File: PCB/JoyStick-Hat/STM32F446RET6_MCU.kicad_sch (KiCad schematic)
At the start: 51 parts, among them J1 20021121-00010C4LF, J16 Conn_01x06, J2 BU2032SM-JJ-GTR, J3 0675031020, SW1 TL3301NF260QG, U1 STM32F446VETx, X1 ABM3B-8.000MHZ-B2-T, X2 ABS07-32.768KHZ-9-T

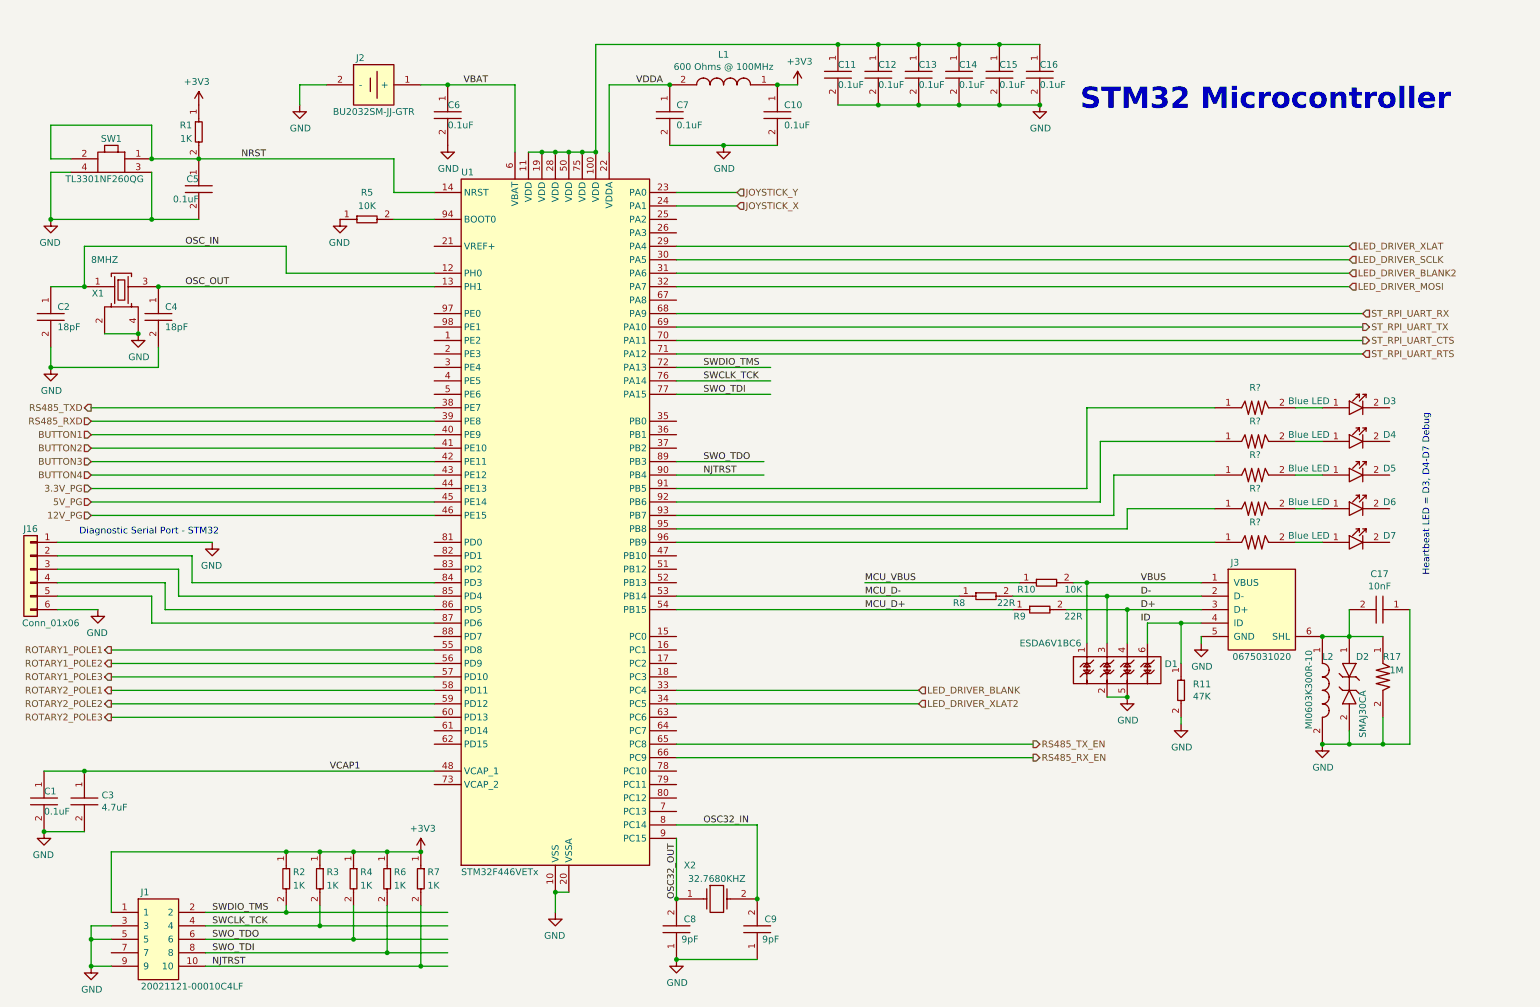
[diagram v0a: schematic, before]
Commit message: Design Rules, Component Placement. Features Dropped
Added design rules for OSHPark.com to PCB, Most components placed roughly for whole board more to follow and more tweaks,. Features were dropped/rearanged. USB for STM32 dropped as its not necessary. LED driver and LEDs will be on separate board and SPI will run through cabling via differential transceiver that has yet to be added to schematic.
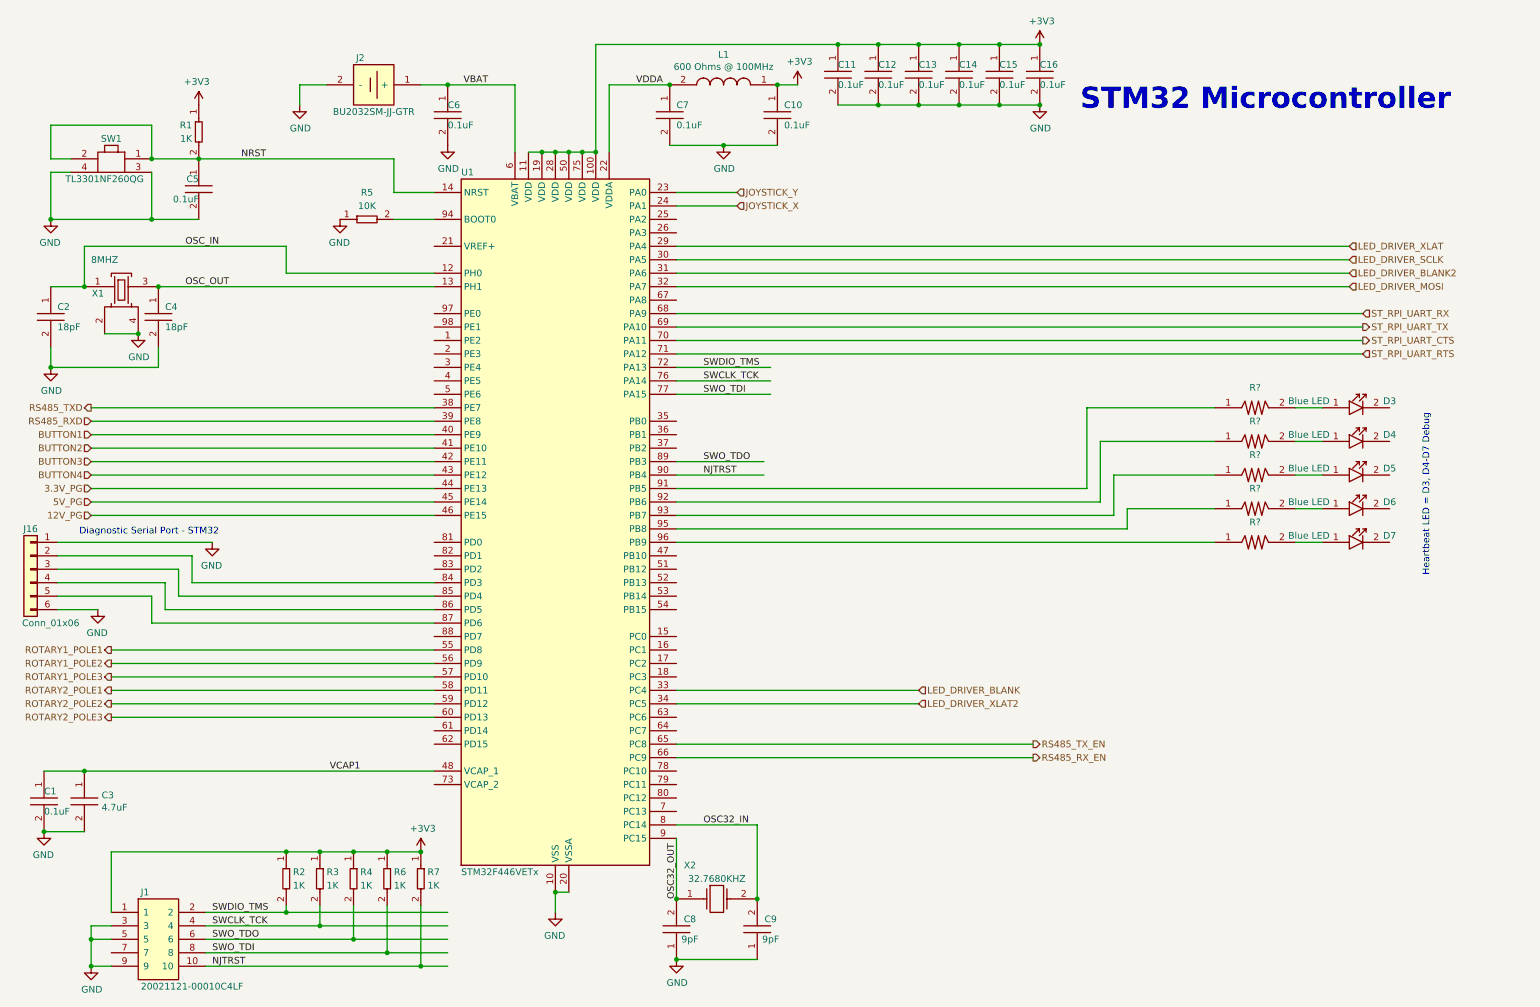
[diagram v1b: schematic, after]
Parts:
- removed C17: C0603X103K1RAC3316, AVR-KiCAD-Lib-Capacitors:C0603, symbol AVR-KiCAD-Lib-Capacitors:C0603X103K1RAC3316
- removed D1: ESDA6V1BC6, AVR-KiCAD-Lib-ICs:SOT-23-6_Handsoldering, symbol AVR-KiCAD-Lib-Diodes:ESDA6V1BC6
- removed D2: SMAJ30CA, AVR-KiCAD-Lib-Diodes:SMAJ30CA, symbol AVR-KiCAD-Lib-Diodes:SMAJ30CA
- removed J3: 0675031020, AVR-KiCAD-Lib-Connectors:USB_Mini-B, symbol AVR-KiCAD-Lib-Connectors:0675031020
- removed L2: MI0603K300R-10, AVR-KiCAD-Lib-Inductors:MI0603K300R-10, symbol AVR-KiCAD-Lib-Inductors:MI0603K300R-10
- removed R10: RC0402FR-0710KL, AVR-KiCAD-Lib-Resistors:R0402, symbol AVR-KiCAD-Lib-Resistors:RC0402FR-0710KL
- removed R11: RC0603FR-0747KL, AVR-KiCAD-Lib-Resistors:R0603, symbol AVR-KiCAD-Lib-Resistors:RC0603FR-0747KL
- removed R17: RC1206FR-071ML, AVR-KiCAD-Lib-Resistors:R1206, symbol AVR-KiCAD-Lib-Resistors:RC1206FR-071ML
- removed R8, R9: RC0402FR-0722RL, AVR-KiCAD-Lib-Resistors:R0402, symbol AVR-KiCAD-Lib-Resistors:RC0402FR-0722RL
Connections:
- net +3V3: now also C11.1, C12.1, C13.1, C14.1, C15.1, C16.1, U1.100 (VDD), U1.11 (VDD), U1.19 (VDD), U1.28 (VDD), U1.50 (VDD), U1.75 (VDD)
- net MCU_D+: no longer names the net of U1.54 (PB15)
- net MCU_D-: no longer names the net of U1.53 (PB14)

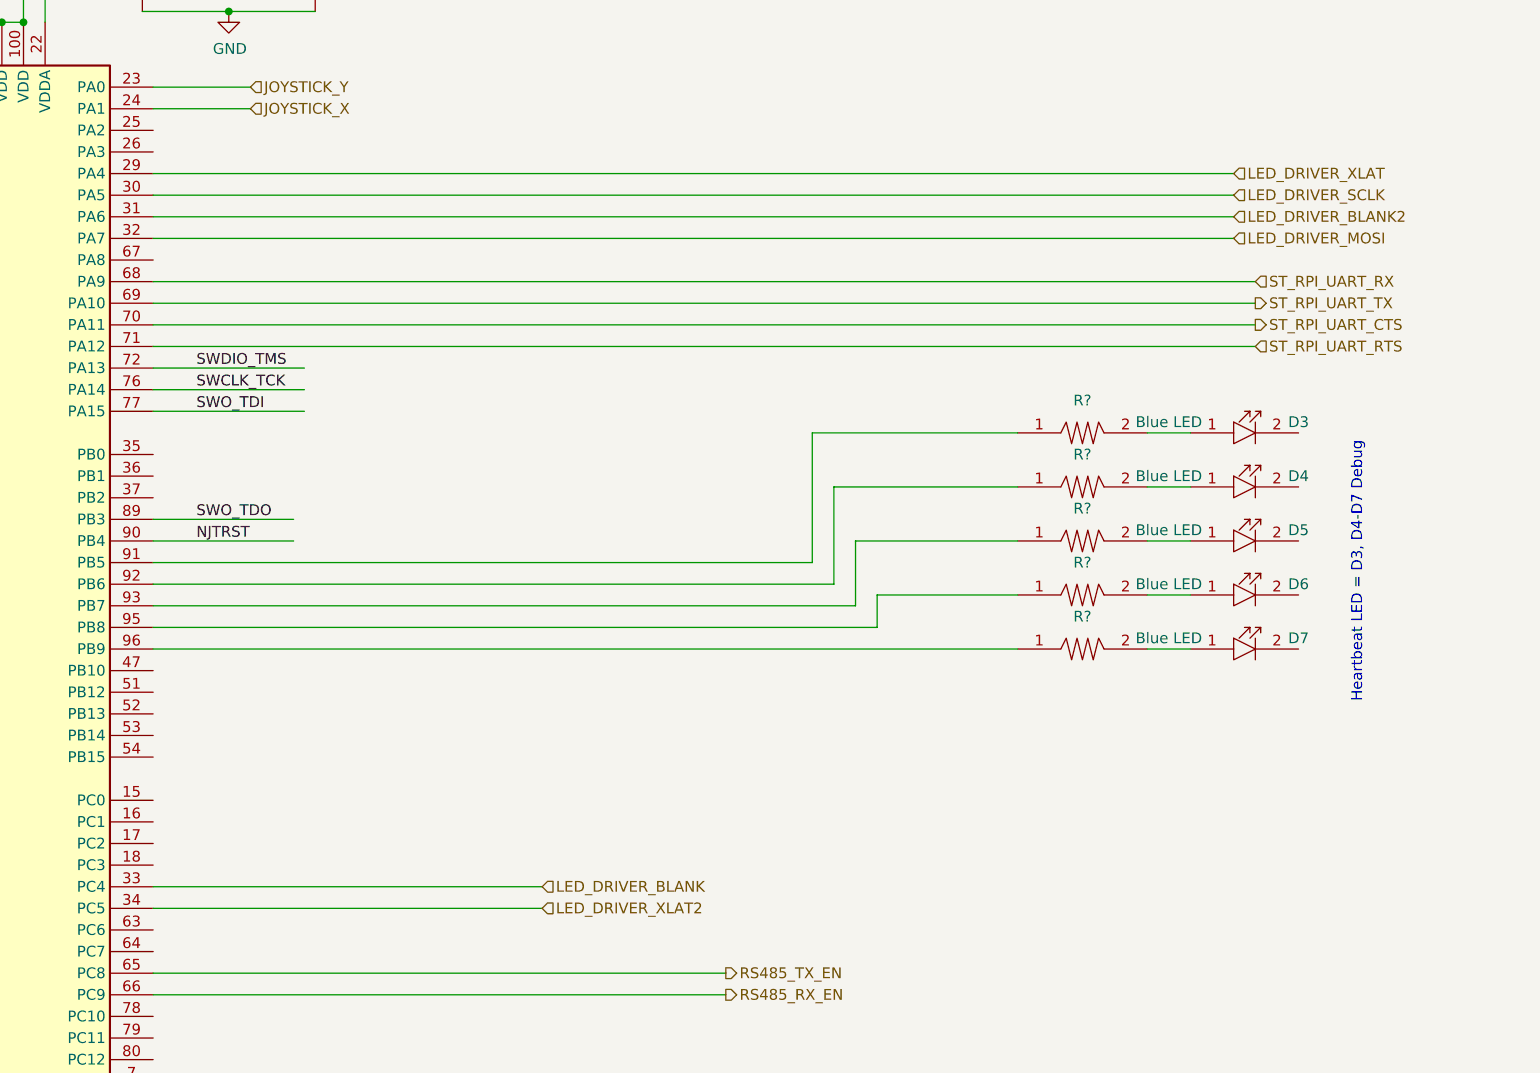
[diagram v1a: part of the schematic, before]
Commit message: Board Tweaks and progress
Made progress with baord. Adjusted the position of RPi header to be correct and absolute. Changed location of regulator modules and power input capacitors. Added 3D models missing from the larger components. Changed connectors and positions for just about everything. Added connnector for LED driver duagher board .
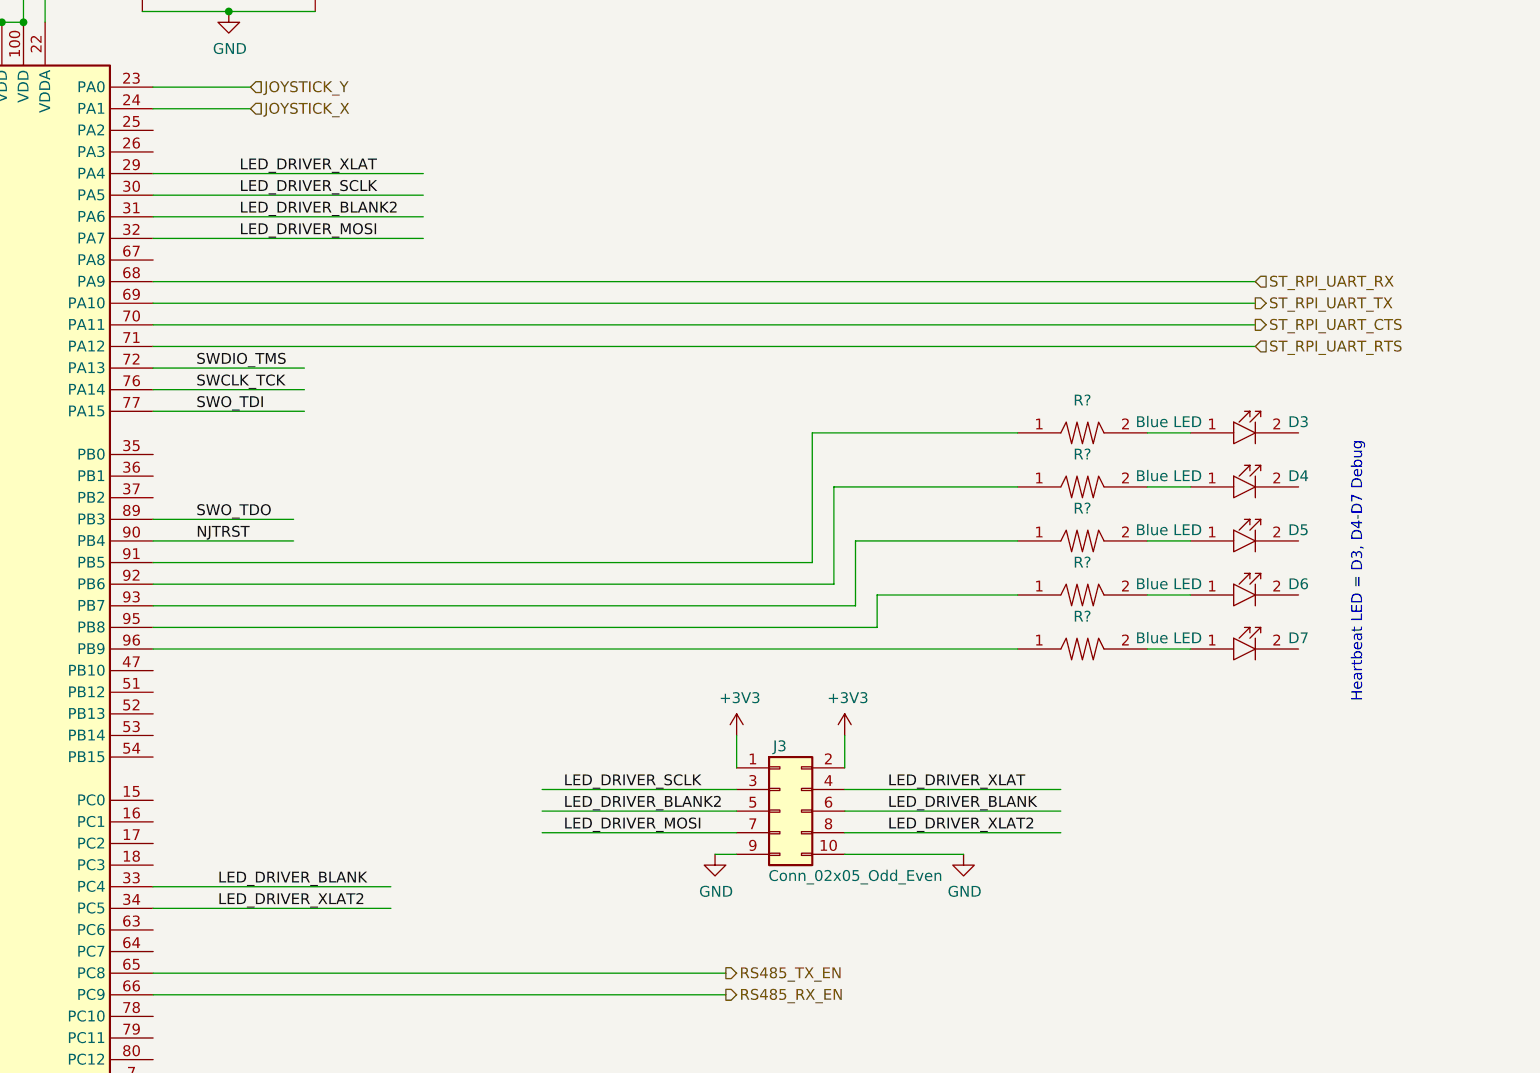
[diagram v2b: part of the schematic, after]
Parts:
- added J3: Conn_02x05_Odd_Even, Connector_PinHeader_2.54mm:PinHeader_2x05_P2.54mm_Vertical, symbol Connector_Generic:Conn_02x05_Odd_Even
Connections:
- net +3V3: now also J3.1 (Pin_1), J3.2 (Pin_2)
- net GND: now also J3.10 (Pin_10), J3.9 (Pin_9)
- net LED_DRIVER_BLANK: now also J3.6 (Pin_6)
- net LED_DRIVER_BLANK2: now also J3.5 (Pin_5)
- net LED_DRIVER_MOSI: now also J3.7 (Pin_7)
- net LED_DRIVER_SCLK: now also J3.3 (Pin_3)
- net LED_DRIVER_XLAT: now also J3.4 (Pin_4)
- net LED_DRIVER_XLAT2: now also J3.8 (Pin_8)
